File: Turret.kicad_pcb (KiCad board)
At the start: 2 copper layers, 104 x 54 mm, 30 parts

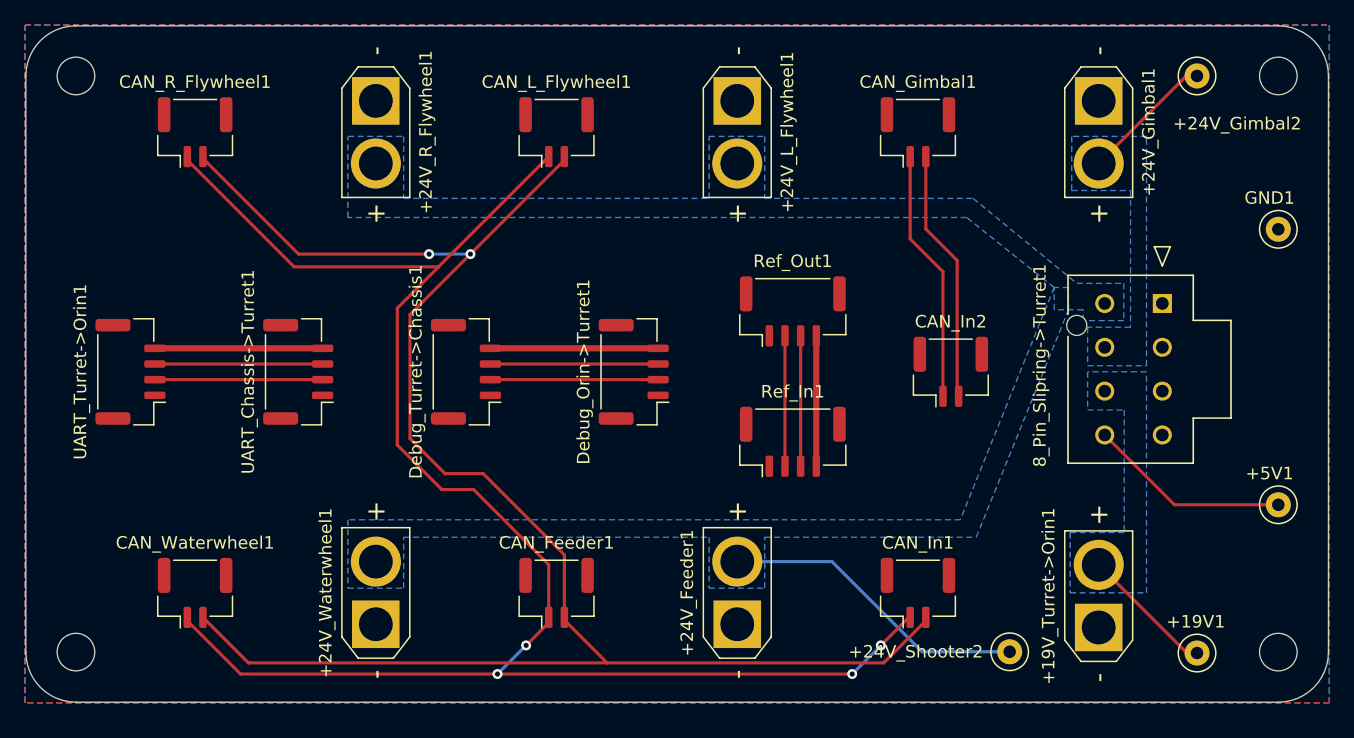
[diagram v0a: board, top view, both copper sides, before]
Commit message: Added a 16 input connector
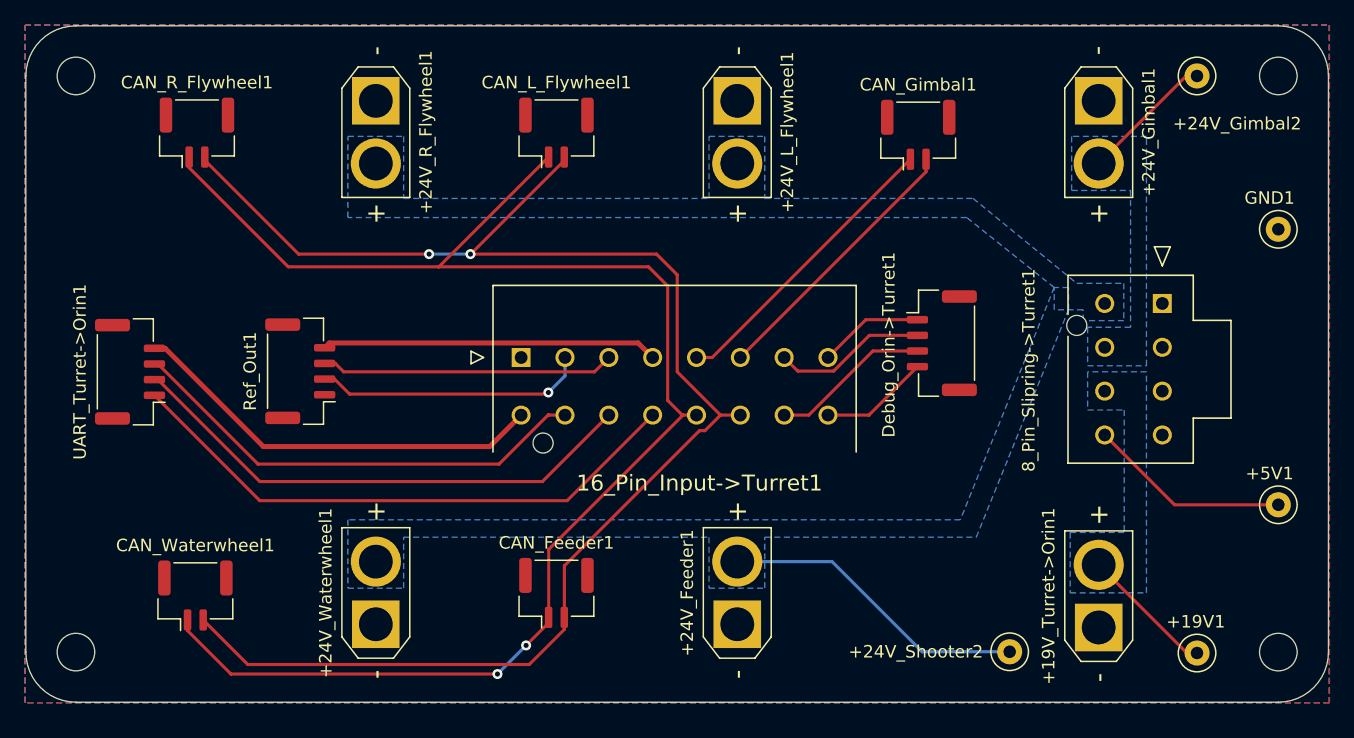
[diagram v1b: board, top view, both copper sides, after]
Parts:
- removed CAN_In1, CAN_In2: Conn_01x02_Pin, Connector_JST:JST_GH_BM02B-GHS-TBT_1x02-1MP_P1.25mm_Vertical
- removed Debug_Turret->Chassis1, Ref_In1, UART_Chassis->Turret1: Conn_01x04_Pin, Connector_JST:JST_GH_BM04B-GHS-TBT_1x04-1MP_P1.25mm_Vertical
- added 16_Pin_Input->Turret1: 172298-1116, Connectors:172298-YY16, F.Cu at (80.0, 60.6)
- +19V_Turret->Orin1, +24V_Feeder1, +24V_Gimbal1, +24V_L_Flywheel1, +24V_R_Flywheel1, +24V_Waterwheel1: footprint Robomaster_ICs:AMASS_XT30U-F_1x02_P5.0mm_Vertical_copy -> Connector_AMASS:AMASS_XT30U-F_1x02_P5.0mm_Vertical
- 8_Pin_Slipring->Turret1: footprint ICs:CON_1722981108_MOL -> Connectors:CON_1722981108_MOL
- moved Ref_Out1 39.6 mm to (62.4, 61.7), turned to 90 degrees
- moved Debug_Orin->Turret1 24.7 mm to (113.6, 59.4), turned to -90 degrees
- moved G*** 9.98 mm to (92.8, 60.6)
- moved CAN_Gimbal1 0.21 mm to (111.7, 42.8)
- moved CAN_Waterwheel1 0.21 mm to (54.0, 79.6)
- moved CAN_R_Flywheel1 0.15 mm to (54.1, 42.6)
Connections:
- Debug_Orin->Turret1 pad 1: GND -> /DebugGND
- UART_Turret->Orin1 pad 1: GND -> /UartGND
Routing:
- net /UartGND: track 0.00 -> 46.1 mm
- net /UART_TX: track 13.4 -> 41.8 mm
- net /UART_RX: track 13.4 -> 37.7 mm
- net /3.3V_UART: track 13.4 -> 33.6 mm
- net /CANL: track 140.0 -> 121.6 mm, vias 4 -> 2
- net /CANH: track 139.4 -> 121.4 mm
- net /Ref_PWR: track 10.4 -> 26.8 mm
- net /CANHRef: track 10.4 -> 23.4 mm
- net /CANLRef: track 10.4 -> 21.8 mm, vias 0 -> 1
- net /DebugGND: track 0.00 -> 8.39 mm
- net /3.3V_Debug: track 13.4 -> 8.74 mm
- net /CANLPitch: track 20.3 -> 23.7 mm
- net /CANHPitch: track 20.2 -> 22.0 mm
- net /SWDIO: track 13.4 -> 12.3 mm
- net /SWCLK: track 13.4 -> 12.8 mm

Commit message: XT30 outputs to ESCs rotated
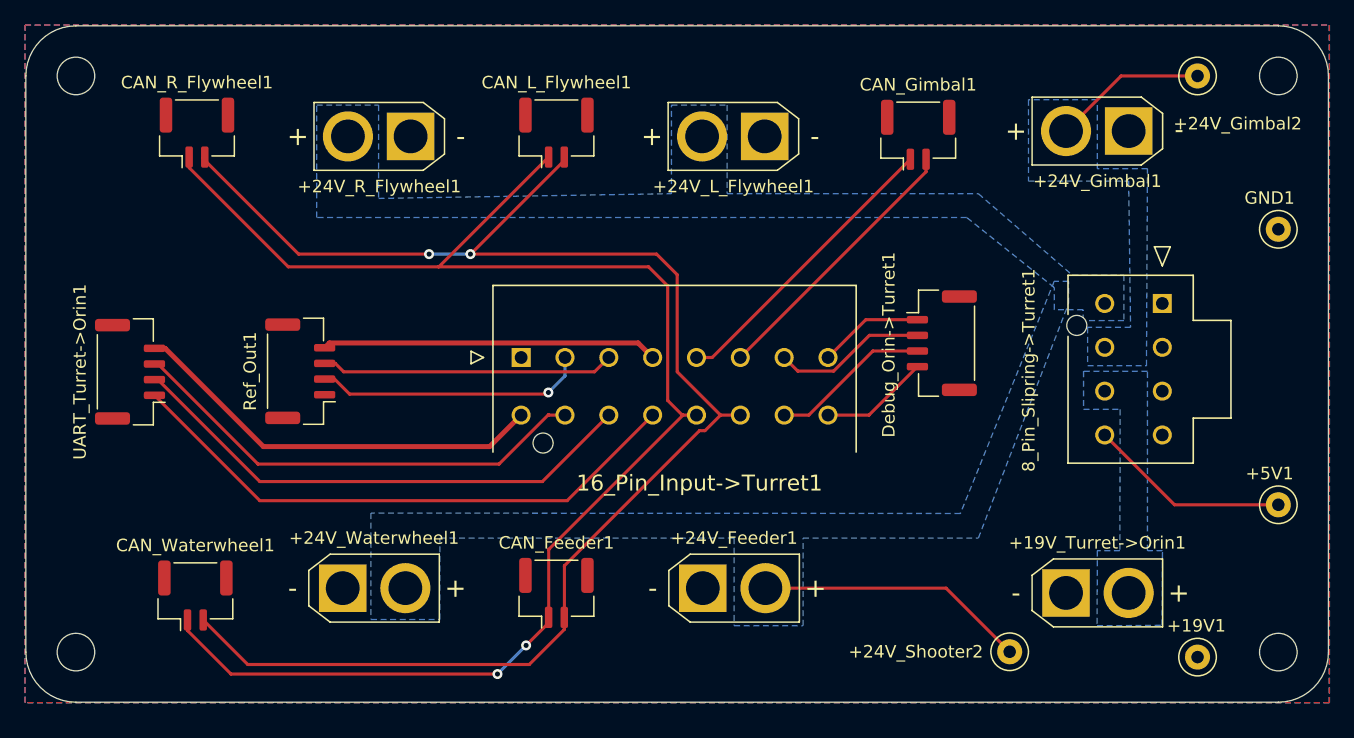
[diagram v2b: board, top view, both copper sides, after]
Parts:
- moved +24V_Feeder1 3.98 mm to (94.5, 79.0), turned to 0 degrees
- moved +24V_R_Flywheel1 3.97 mm to (71.2, 42.9), turned to 180 degrees
- moved +24V_Waterwheel1 3.91 mm to (65.8, 79.0), turned to 0 degrees
- moved +19V_Turret->Orin1 3.80 mm to (123.5, 79.4), turned to 0 degrees
- moved +24V_L_Flywheel1 3.58 mm to (99.4, 42.9), turned to 180 degrees
- moved +24V_Gimbal1 3.40 mm to (128.5, 42.5), turned to 180 degrees
- moved +19V1 0.33 mm to (134.0, 84.5)
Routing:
- net /+19V: track 10.8 -> 0.81 mm
- net /+24V_Shooter: track 24.7 -> 21.6 mm
- net /+24V_Gimbal: track 10.7 -> 12.3 mm

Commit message: Fixed 16-pin and 8-pin netnames for correct connections, updated gerbers
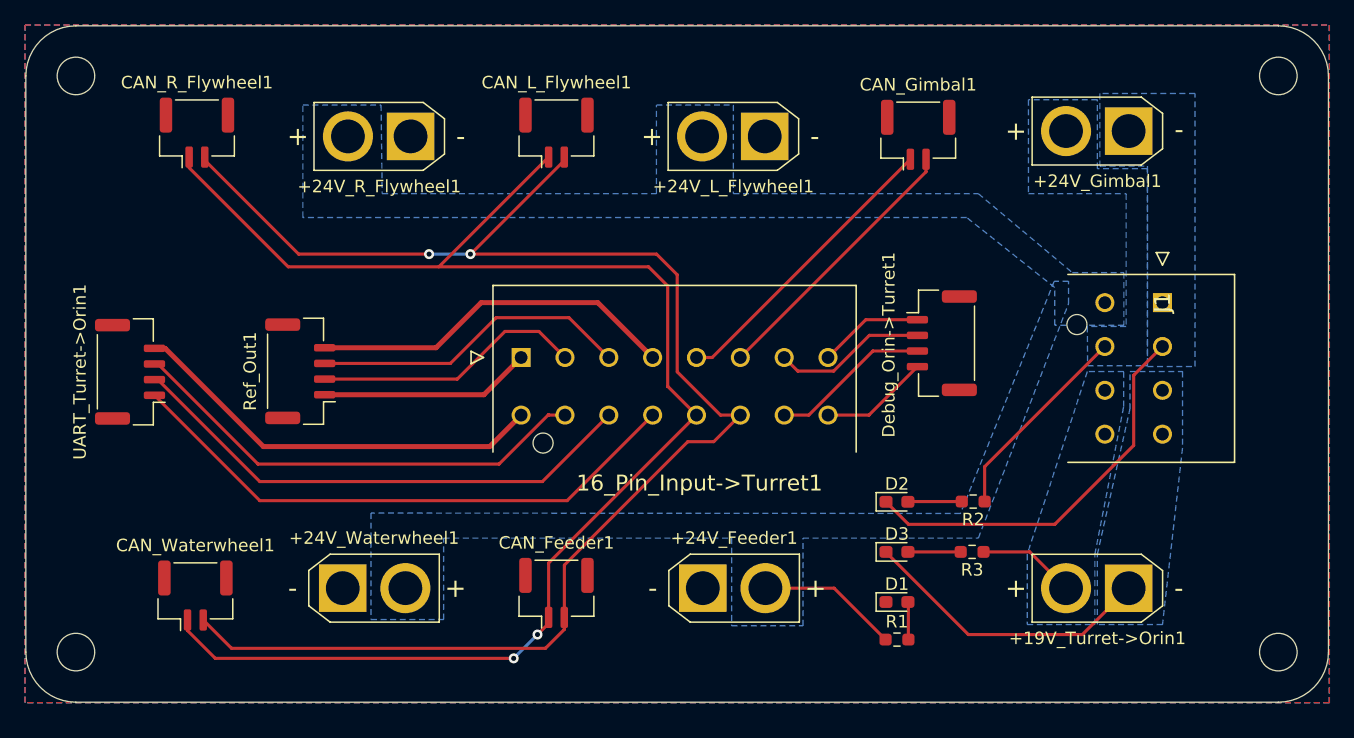
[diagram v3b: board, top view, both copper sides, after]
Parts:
- removed +19V1, +24V_Gimbal2, +24V_Shooter2, +5V1, GND1: TestPoint, TestPoint:TestPoint_Loop_D1.80mm_Drill1.0mm_Beaded
- removed 8_Pin_Slipring->Turret1: Conn_01x08_Pin, Connectors:CON_1722981108_MOL
- added D1: 150060YS75000, LED_SMD:LED_0603_1608Metric_Pad1.05x0.95mm_HandSolder, F.Cu at (110.0, 80.1)
- added D2: 150060YS75000, LED_SMD:LED_0603_1608Metric_Pad1.05x0.95mm_HandSolder, F.Cu at (110.0, 72.1)
- added D3: 150060YS75000, LED_SMD:LED_0603_1608Metric_Pad1.05x0.95mm_HandSolder, F.Cu at (110.0, 76.1)
- added J1: 172298-1108, Connectors:172298-YY08, F.Cu at (131.2, 56.2)
- added R1: 1k, Resistor_SMD:R_0603_1608Metric_Pad0.98x0.95mm_HandSolder, F.Cu at (110.0, 83.1)
- added R2: 1k, Resistor_SMD:R_0603_1608Metric_Pad0.98x0.95mm_HandSolder, F.Cu at (116.1, 72.1)
- added R3: 1k, Resistor_SMD:R_0603_1608Metric_Pad0.98x0.95mm_HandSolder, F.Cu at (116.0, 76.1)
- moved +19V_Turret->Orin1 5.01 mm to (128.5, 79.0), turned to 180 degrees
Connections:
- net /3.3V_Debug renamed /SWD_3V3
- net /3.3V_UART renamed /UART_3V3
- net /CANHPitch renamed /CANGim_H
- net /CANHRef renamed /Ref_CANH
- net /CANLPitch renamed /CANGim_L
- net /CANLRef renamed /Ref_CANL
- net /DebugGND renamed /SWD_GND
- net /SWCLK renamed /SWD_SWCLK
- net /SWDIO renamed /SWD_SWDIO
- net /UartGND renamed /UART_GND
- +19V_Turret->Orin1 pad 1: GND -> /Orin_PWR_GND
- +24V_Feeder1 pad 1: GND -> /Shooter_PWR_GND
- +24V_Gimbal1 pad 1: GND -> /Gimbal_PWR_GND
- +24V_L_Flywheel1 pad 1: GND -> /Shooter_PWR_GND
- +24V_R_Flywheel1 pad 1: GND -> /Shooter_PWR_GND
- +24V_Waterwheel1 pad 1: GND -> /Shooter_PWR_GND
- 16_Pin_Input->Turret1 pad 1: GND -> /Ref_GND
- Ref_Out1 pad 1: GND -> /Ref_GND
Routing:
- net /Gimbal_PWR_GND: track 0.00 -> 32.0 mm
- net /Orin_PWR_GND: track 0.00 -> 23.7 mm
- net /Ref_GND: track 0.00 -> 16.9 mm
- net /+5V: track 16.2 -> 0.00 mm
- net /+24V_Shooter: track 21.6 -> 11.3 mm
- net /+19V: track 0.81 -> 7.79 mm
- net Net-(D2-A): track 0.00 -> 4.31 mm
- net Net-(D3-A): track 0.00 -> 4.21 mm
- net /+24V_Gimbal: track 12.3 -> 16.4 mm
- net Net-(D1-A): track 0.00 -> 3.02 mm
- net /Ref_PWR: track 26.8 -> 29.5 mm
- net /Ref_CANH: track 23.4 -> 25.5 mm
- net /CANL: track 121.6 -> 120.4 mm
- net /CANH: track 121.4 -> 122.0 mm
- net /Ref_CANL: track 21.8 -> 21.6 mm, vias 1 -> 0
- added copper zone on B.Cu, net /Gimbal_PWR_GND
- added copper zone on B.Cu, net /Orin_PWR_GND
- added copper zone on B.Cu, net /Shooter_PWR_GND
- added copper zone on F.Cu, net /Shooter_PWR_GND
- removed copper zone on B.Cu, net GND
- removed copper zone on F.Cu, net GND

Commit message: Updated fab files
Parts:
- removed 16_Pin_Input->Turret1: 172298-1116, Connectors:172298-YY16
- removed G***: LOGO, LOGO
- added J2: 501645-1620, Connectors:5016451620, F.Cu at (92.2, 62.5)
- moved UART_Turret->Orin1 20.4 mm to (68.6, 66.7)
- moved Ref_Out1 9.80 mm to (53.4, 57.7)
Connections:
- Ref_Out1 pad 2: /Ref_CANL -> /Ref_CAN-
- Ref_Out1 pad 3: /Ref_CANH -> /Ref_CAN+
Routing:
- net /Ref_CAN+: track 0.00 -> 36.5 mm
- net /Ref_CAN-: track 0.00 -> 34.0 mm
- net /Ref_CANH: track 25.5 -> 0.00 mm
- net /UART_GND: track 46.1 -> 24.4 mm
- net /Ref_CANL: track 21.6 -> 0.00 mm
- net /UART_TX: track 41.8 -> 21.8 mm
- net /UART_RX: track 37.7 -> 19.3 mm
- net /UART_3V3: track 33.6 -> 16.8 mm
- net /Ref_GND: track 16.9 -> 31.4 mm
- net /Ref_PWR: track 29.5 -> 39.0 mm
- net /SWD_3V3: track 8.74 -> 15.0 mm
- net /SWD_GND: track 8.39 -> 14.5 mm
- net /CANH: track 122.0 -> 127.2 mm
- net /CANL: track 120.4 -> 123.3 mm, vias 2 -> 3
- net /CANGim_H: track 22.0 -> 22.6 mm
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
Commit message: Updated fab files
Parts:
- J1: footprint Connectors:172298-YY08 -> Robomaster_Connectors:172298-YY08
- J2: footprint Connectors:5016451620 -> Robomaster_Connectors:5016451620
